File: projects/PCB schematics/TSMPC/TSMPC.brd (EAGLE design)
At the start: 81.3 x 70 mm, 23 parts, among them J1 2P_1-770166-0, J2 2P_1-770166-0, J3 2P_1-770166-0

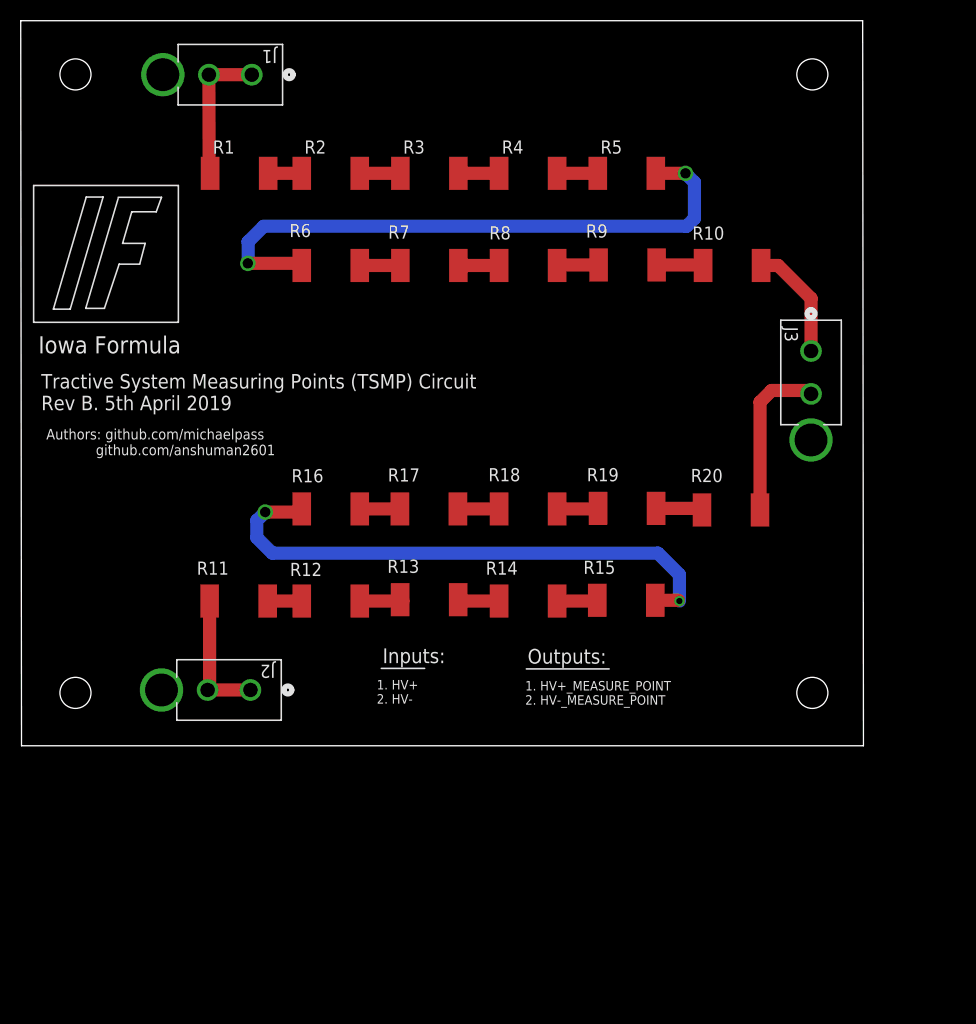
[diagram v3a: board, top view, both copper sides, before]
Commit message: TSMPC - DRC error. Ready for final PR#3 reviewal.
Squash - TSMPC - DRC fixes. Output connector polarity labeled.
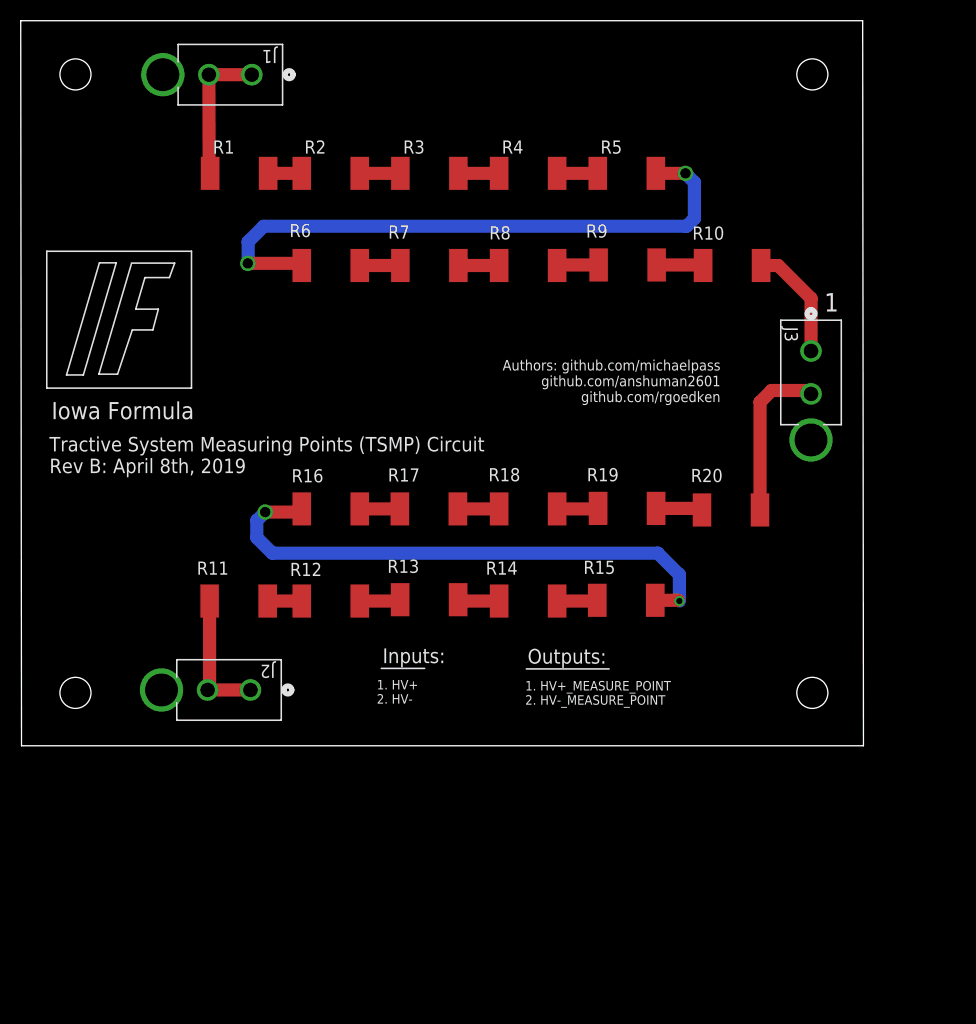
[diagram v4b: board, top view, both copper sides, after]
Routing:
- net HV-: track 14.0 -> 12.8 mm
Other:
- board text added: "1"
- board text added: "Authors: github.com/michaelpass github.com/anshuman2601 github.com/rgoedken"
- board text added: "Tractive System Measuring Points (TSMP) Circuit Rev B: April 8th, 2019"
- board text removed: "Authors: github.com/michaelpass github.com/anshuman2601"
- board text removed: "Tractive System Measuring Points (TSMP) Circuit Rev B. 5th April 2019"
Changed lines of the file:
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@@
 <wire x1="81.1838" y1="69.9772" x2="-0.0762" y2="69.9772" width="0" layer="20"/>
 <wire x1="-0.0762" y1="69.9772" x2="0" y2="0" width="0" layer="20"/>
-<wire x1="1.1684" y1="54.0766" x2="1.1684" y2="40.8686" width="0.1524" layer="25"/>
-<wire x1="1.1684" y1="40.8686" x2="15.1384" y2="40.8686" width="0.1524" layer="25"/>
-<wire x1="15.1384" y1="40.8686" x2="15.1384" y2="54.0766" width="0.1524" layer="25"/>
-<wire x1="15.1384" y1="54.0766" x2="1.1684" y2="54.0766" width="0.1524" layer="25"/>
-<wire x1="6.2484" y1="52.959" x2="3.0734" y2="42.1386" width="0.1524" layer="255"/>
-<wire x1="6.2484" y1="52.959" x2="3.0734" y2="42.1386" width="0.1524" layer="25"/>
-<wire x1="3.0734" y1="42.1386" x2="4.699" y2="42.1386" width="0.1524" layer="25"/>
-<wire x1="4.699" y1="42.1386" x2="7.874" y2="52.959" width="0.1524" layer="25"/>
-<wire x1="7.874" y1="52.959" x2="6.2484" y2="52.959" width="0.1524" layer="25"/>
-<wire x1="9.3218" y1="52.8066" x2="6.1976" y2="42.2148" width="0.1524" layer="25"/>
-<wire x1="6.1976" y1="42.2148" x2="8.001" y2="42.2148" width="0.1524" layer="25"/>
-<wire x1="8.001" y1="42.2148" x2="9.4234" y2="46.482" width="0.1524" layer="25"/>
-<wire x1="9.4234" y1="46.482" x2="11.4046" y2="46.482" width="0.1524" layer="25"/>
-<wire x1="11.4046" y1="46.482" x2="11.938" y2="48.4886" width="0.1524" layer="25"/>
-<wire x1="11.938" y1="48.4886" x2="9.7536" y2="48.4886" width="0.1524" layer="25"/>
-<wire x1="9.7536" y1="48.4886" x2="10.6426" y2="51.5366" width="0.1524" layer="25"/>
-<wire x1="10.6426" y1="51.5366" x2="13.0048" y2="51.5366" width="0.1524" layer="25"/>
-<wire x1="13.0048" y1="51.5366" x2="13.5128" y2="52.9336" width="0.1524" layer="25"/>
-<wire x1="13.5128" y1="52.9336" x2="9.3218" y2="52.9336" width="0.1524" layer="25"/>
-<text x="1.6256" y="37.8714" size="1.651" layer="25" font="vector">Iowa Formula</text>
-<text x="1.905" y="32.385" size="1.397" layer="25" font="vector">Tractive System Measuring Points (TSMP) Circuit
-Rev B. 5th April 2019</text>
-<text x="2.3876" y="24.9936" size="1.016" layer="25" font="vector">Authors: github.com/michaelpass
+<wire x1="2.4384" y1="47.7266" x2="2.4384" y2="34.5186" width="0.1524" layer="25"/>
+<wire x1="2.4384" y1="34.5186" x2="16.4084" y2="34.5186" width="0.1524" layer="25"/>
+<wire x1="16.4084" y1="34.5186" x2="16.4084" y2="47.7266" width="0.1524" layer="25"/>
+<wire x1="16.4084" y1="47.7266" x2="2.4384" y2="47.7266" width="0.1524" layer="25"/>
+<wire x1="7.5184" y1="46.609" x2="4.3434" y2="35.7886" width="0.1524" layer="255"/>
+<wire x1="7.5184" y1="46.609" x2="4.3434" y2="35.7886" width="0.1524" layer="25"/>
+<wire x1="4.3434" y1="35.7886" x2="5.969" y2="35.7886" width="0.1524" layer="25"/>
+<wire x1="5.969" y1="35.7886" x2="9.144" y2="46.609" width="0.1524" layer="25"/>
+<wire x1="9.144" y1="46.609" x2="7.5184" y2="46.609" width="0.1524" layer="25"/>
+<wire x1="10.5918" y1="46.4566" x2="7.4676" y2="35.8648" width="0.1524" layer="25"/>
+<wire x1="7.4676" y1="35.8648" x2="9.271" y2="35.8648" width="0.1524" layer="25"/>
+<wire x1="9.271" y1="35.8648" x2="10.6934" y2="40.132" width="0.1524" layer="25"/>
+<wire x1="10.6934" y1="40.132" x2="12.6746" y2="40.132" width="0.1524" layer="25"/>
+<wire x1="12.6746" y1="40.132" x2="13.208" y2="42.1386" width="0.1524" layer="25"/>
+<wire x1="13.208" y1="42.1386" x2="11.0236" y2="42.1386" width="0.1524" layer="25"/>
+<wire x1="11.0236" y1="42.1386" x2="11.9126" y2="45.1866" width="0.1524" layer="25"/>
+<wire x1="11.9126" y1="45.1866" x2="14.2748" y2="45.1866" width="0.1524" layer="25"/>
+<wire x1="14.2748" y1="45.1866" x2="14.7828" y2="46.5836" width="0.1524" layer="25"/>
+<wire x1="14.7828" y1="46.5836" x2="10.5918" y2="46.5836" width="0.1524" layer="25"/>
+<text x="2.8956" y="31.5214" size="1.651" layer="25" font="vector">Iowa Formula</text>
+<text x="2.6924" y="26.3144" size="1.397" layer="25" font="vector">Tractive System Measuring Points (TSMP) Circuit
+Rev B: April 8th, 2019</text>
+<text x="67.4624" y="37.2364" size="1.016" layer="25" font="vector" rot="R180">Authors: github.com/michaelpass
             github.com/anshuman2601
+            github.com/rgoedken
              </text>
 <hole x="5.207" y="64.7954" drill="3"/>
@@
 <wire x1="34.7218" y1="7.4676" x2="38.9128" y2="7.4676" width="0.1524" layer="25"/>
 <wire x1="48.7172" y1="7.4168" x2="56.7182" y2="7.4168" width="0.1524" layer="25"/>
+<text x="77.47" y="41.91" size="1.778" layer="25">1</text>
 </plain>
 <attributes>
@@
 <signal name="HV+">
 <contactref element="R1" pad="1"/>
-<wire x1="18.4658" y1="55.245" x2="18.2058" y2="55.245" width="0.1524" layer="1"/>
 <contactref element="J1" pad="2"/>
 <contactref element="J1" pad="1"/>
@@
 <signal name="HV-">
 <contactref element="R11" pad="1"/>
-<wire x1="17.78" y1="13.97" x2="18.155" y2="13.97" width="0.1524" layer="1"/>
 <contactref element="J2" pad="2"/>
 <contactref element="J2" pad="1"/>
-<wire x1="22.098" y1="5.3848" x2="17.9578" y2="5.3848" width="1.27" layer="1"/>
-<wire x1="17.9578" y1="5.3848" x2="18.0772375" y2="5.5042375" width="1.27" layer="1"/>
-<wire x1="18.248328125" y1="13.501671875" x2="17.78" y2="13.97" width="0.8128" layer="1"/>
+<wire x1="17.9578" y1="5.3848" x2="22.098" y2="5.3848" width="1.27" layer="1"/>
 <wire x1="18.155" y1="13.97" x2="18.155" y2="5.582" width="1.27" layer="1"/>
-<wire x1="18.155" y1="5.582" x2="17.9578" y2="5.3848" width="0.8128" layer="1"/>
+<wire x1="18.155" y1="5.582" x2="17.9578" y2="5.3848" width="1.27" layer="1"/>
 </signal>
 <signal name="N$22">
 <contactref element="R12" pad="2"/>
 <contactref element="R13" pad="1"/>
-<wire x1="32.645" y1="13.97" x2="36.83" y2="13.97" width="1.27" layer="1"/>
-<wire x1="36.83" y1="13.97" x2="36.5446" y2="14.097" width="0" layer="19" extent="1-1"/>
+<wire x1="32.645" y1="13.97" x2="36.4176" y2="13.97" width="1.27" layer="1"/>
+<wire x1="36.4176" y1="13.97" x2="36.5446" y2="14.097" width="0.8128" layer="1"/>
 </signal>
 <signal name="N$23">
@@
 <contactref element="R15" pad="2"/>
 <contactref element="R16" pad="1"/>
-<wire x1="60.9092" y1="14.0462" x2="61.1692" y2="14.0462" width="0.1524" layer="1"/>
 <wire x1="61.1692" y1="14.0462" x2="63.4238" y2="14.0462" width="1.27" layer="1"/>
 <wire x1="63.4238" y1="14.0462" x2="63.5" y2="13.97" width="0.8128" layer="1"/>
@@
 <contactref element="R16" pad="2"/>
 <contactref element="R17" pad="1"/>
-<wire x1="33.02" y1="22.86" x2="32.645" y2="22.86" width="0.1524" layer="1"/>
 <wire x1="32.645" y1="22.86" x2="36.5192" y2="22.86" width="1.27" layer="1"/>
 </signal>
@@
 <contactref element="R17" pad="2"/>
 <contactref element="R18" pad="1"/>
-<wire x1="42.4942" y1="22.86" x2="42.1192" y2="22.86" width="0.1524" layer="1"/>
 <wire x1="42.1192" y1="22.86" x2="46.095" y2="22.86" width="1.27" layer="1"/>
 </signal>
